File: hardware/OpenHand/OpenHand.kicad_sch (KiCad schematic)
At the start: 0 parts

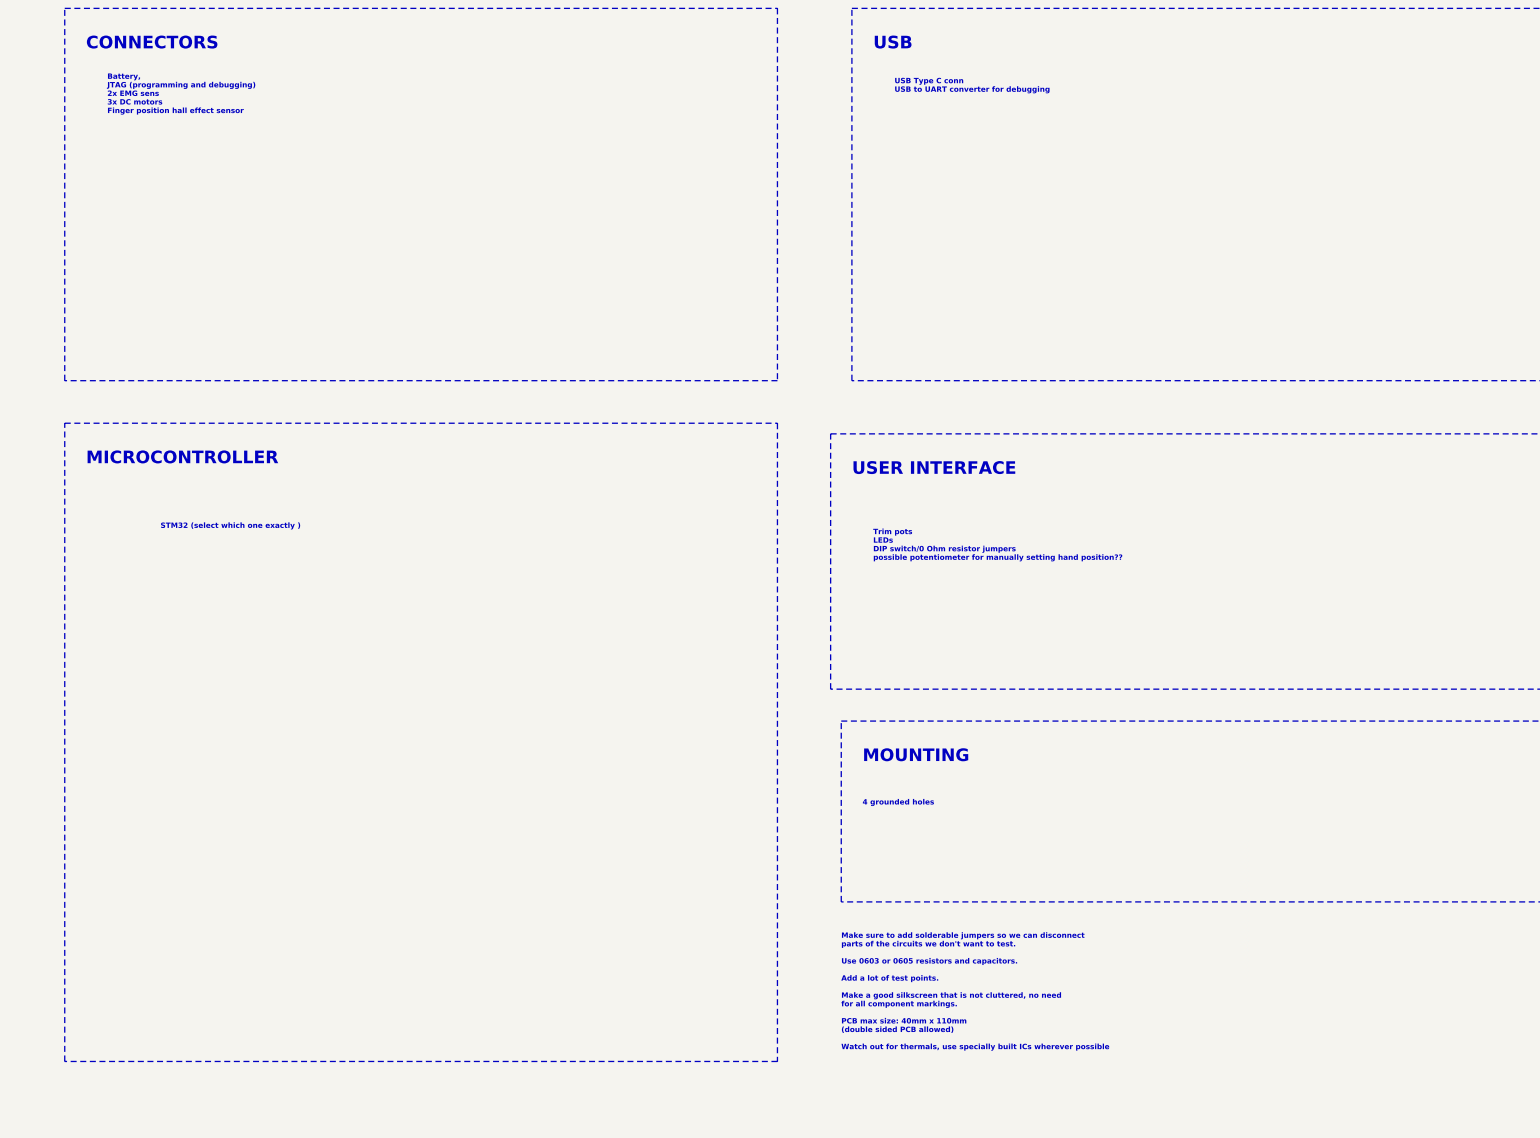
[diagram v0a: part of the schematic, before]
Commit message: Started adding ICs to schematic
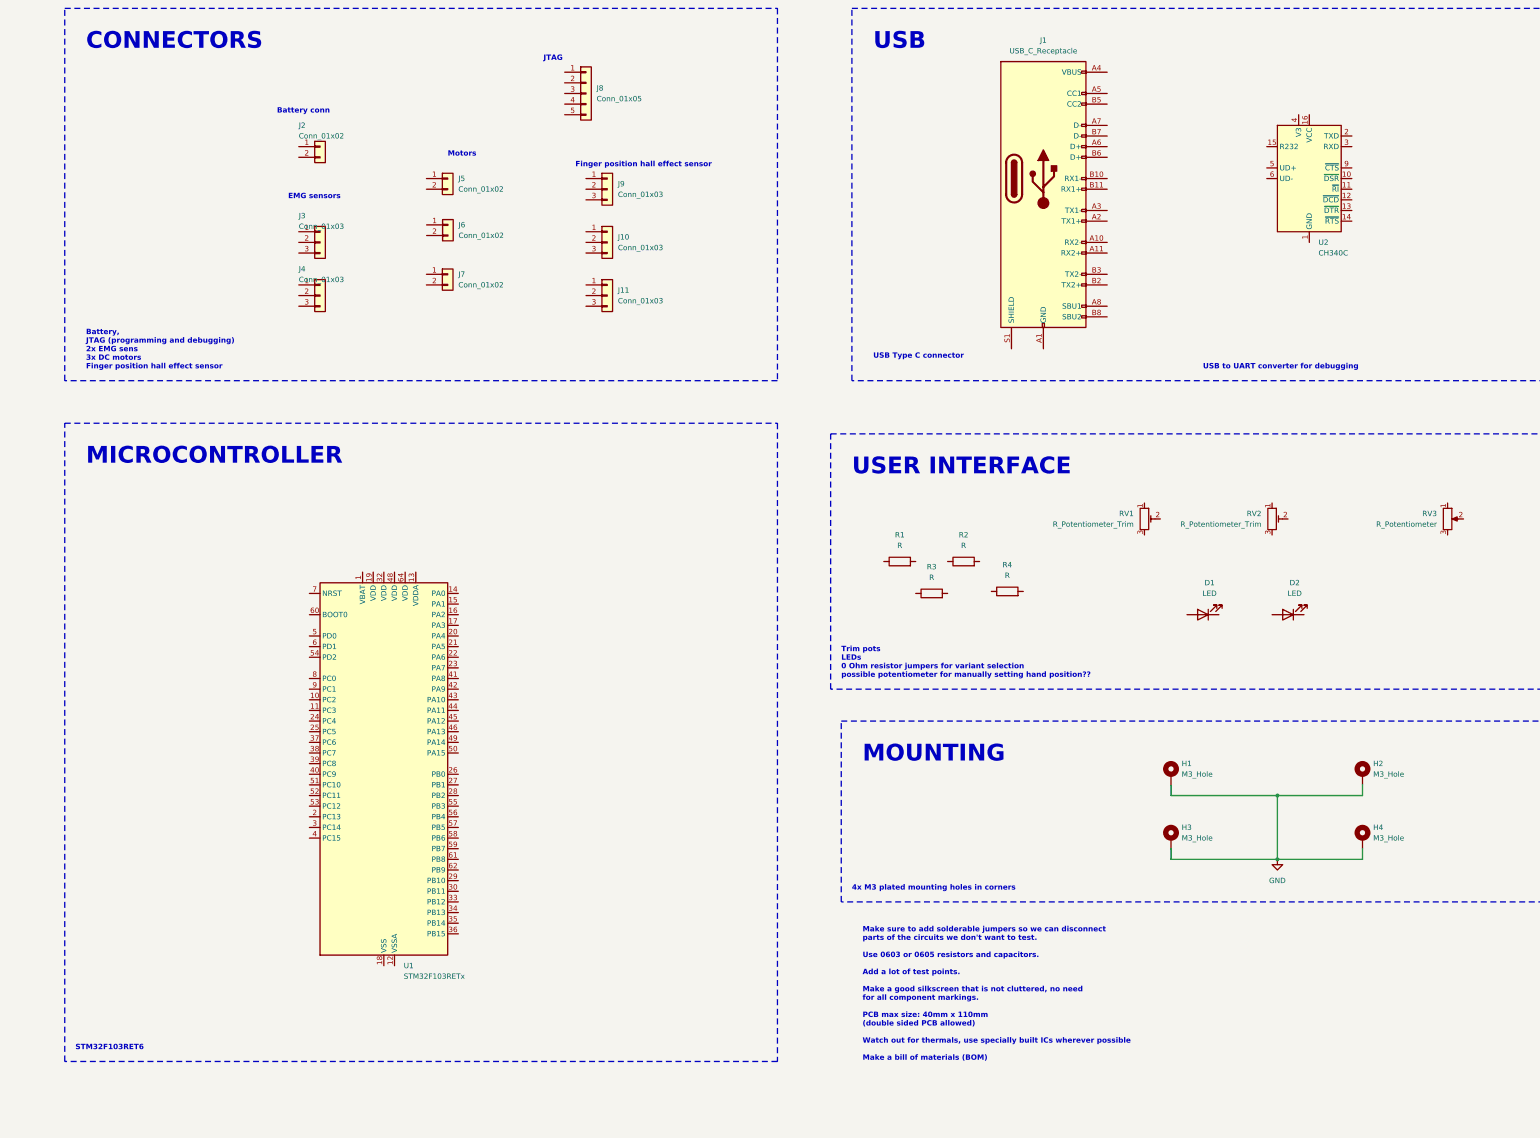
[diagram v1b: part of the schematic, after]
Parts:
- added D1, D2: LED, symbol Device:LED
- added H1, H2, H3, H4: M3_Hole, symbol Mechanical:MountingHole_Pad
- added J1: USB_C_Receptacle, symbol Connector:USB_C_Receptacle
- added J10, J11, J3, J4, J9: Conn_01x03, symbol Connector_Generic:Conn_01x03
- added J2, J5, J6, J7: Conn_01x02, symbol Connector_Generic:Conn_01x02
- added J8: Conn_01x05, symbol Connector_Generic:Conn_01x05
- added R1, R2, R3, R4: R, symbol Device:R
- added RV1, RV2: R_Potentiometer_Trim, symbol Device:R_Potentiometer_Trim
- added RV3: R_Potentiometer, symbol Device:R_Potentiometer
- added U1: STM32F103RETx, Package_QFP:LQFP-64_10x10mm_P0.5mm, symbol MCU_ST_STM32F1:STM32F103RETx
- added U2: CH340C, Package_SO:SOIC-16_3.9x9.9mm_P1.27mm, symbol Interface_USB:CH340C
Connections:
- new net: J1.A1 (GND), J1.A12 (GND), J1.B1 (GND), J1.B12 (GND)
- new net: J1.A4 (VBUS), J1.A9 (VBUS), J1.B4 (VBUS), J1.B9 (VBUS)
- new net: U1.18 (VSS), U1.31 (VSS), U1.47 (VSS), U1.63 (VSS)
- new net GND: H1.1, H2.1, H3.1, H4.1
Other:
- note added: "4x M3 plated mounting holes in corners"
- note added: "Battery conn"
- note added: "EMG sensors"
- note added: "Finger position hall effect sensor"
- note added: "JTAG"
- note added: "Make sure to add solderable jumpers so we can disconnect parts of the circuits we don't want to test. Use 0603 or 0605 resistors and capacitors. Add a lot of test points. Make a good silkscreen that is not cluttered, no need for all component markings. PCB max size: 40mm x 110mm (double sided PCB allowed) Watch out for thermals, use specially built ICs wherever possible Make a bill of materials (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"
- note added: "Motors"
- note added: "STM32F103RET6"
- note added: "Trim pots LEDs 0 Ohm resistor jumpers for variant selection possible potentiometer for manually setting hand position??"
- note added: "USB Type C connector"
- note added: "USB to UART converter for debugging"
- note removed: "4 grounded holes"
- note removed: "Make sure to add solderable jumpers so we can disconnect parts of the circuits we don't want to test. Use 0603 or 0605 resistors and capacitors. Add a lot of test points. Make a good silkscreen that is not cluttered, no need for all component markings. PCB max size: 40mm x 110mm (double sided PCB allowed) Watch out for thermals, use specially built ICs wherever possible"
- note removed: "STM32 (select which one exactly )"
- note removed: "Trim pots LEDs DIP switch/0 Ohm resistor jumpers possible potentiometer for manually setting hand position??"
- note removed: "USB Type C conn USB to UART converter for debugging"

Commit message: Update schematic
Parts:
- removed J8: Conn_01x05, symbol Connector_Generic:Conn_01x05
- added C1: 1u, symbol Device:C
- added C2, C3: 100n, symbol Device:C
- added J9: CONN_JTAG, symbol Connector_Generic:Conn_01x06
- added R5, R6: 1k, symbol Device:R
- added SW1: BTN_RST, symbol Switch:SW_Push
- added SW2: BTN_BOOT, symbol Switch:SW_Push
- added SW3: SW_Push, symbol Switch:SW_Push
- D1: value LED -> RED
- D2: value LED -> GREEN
- J1: renamed from J5; value Conn_01x02 -> CONN_MOTOR_1
- J10: renamed from J4; value Conn_01x03 -> CONN_EMG_2
- J11: value Conn_01x03 -> CONN_POS_3
- J2: renamed from J6; value Conn_01x02 -> CONN_MOTOR_2
- J3: renamed from J2; value Conn_01x02 -> CONN_BATT
- J5: renamed from J9; value Conn_01x03 -> CONN_POS_1
- J6: renamed from J7; value Conn_01x02 -> CONN_MOTOR_3
- J7: renamed from J3; value Conn_01x03 -> CONN_EMG_1
- J8: renamed from J10; value Conn_01x03 -> CONN_POS_2
- RV1: value R_Potentiometer_Trim -> TRIM_POT_1
- RV2: value R_Potentiometer_Trim -> TRIM_POT_2
- RV3: value R_Potentiometer -> POT_1
- renumbered J1 to J4, R3 to R2, R2 to R3, U2 to U1, U1 to U2
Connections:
- net GND is gone; now on net Earth: H1.1, H2.1, H3.1, H4.1
- net Earth: now reaches J8.1 (Pin_1)
- net Earth: now also J10.1 (Pin_1), J11.1 (Pin_1), J3.1 (Pin_1), J4.A1 (GND), J4.A12 (GND), J4.B1 (GND), J4.B12 (GND), J4.S1 (SHIELD), J5.1 (Pin_1), J7.1 (Pin_1), RV1.1, RV2.1, RV3.1, U1.1 (GND), C1.2, C2.2, J9.1 (Pin_1), R5.2, R6.2
- net HALL_SENS_02_S: now reaches J8.2 (Pin_2)
- net HALL_SENS_02_P: now reaches J8.3 (Pin_3)
- net at D1.1 (K): now also R5.1
- net LED_1: now reaches D1.2 (A)
- net +5V: now reaches J4.A4 (VBUS), J4.A9 (VBUS), J4.B4 (VBUS), J4.B9 (VBUS)
- net +5V: now also U1.16 (VCC), C1.1
- net USB_D_P: now reaches J4.A6 (D+)
- net USB_D_P: now also J4.B6 (D+), U1.5 (UD+)
- net USB_D_N: now reaches J4.A7 (D-)
- net USB_D_N: now also J4.B7 (D-), U1.6 (UD-)
- net at U1.13 (~{DTR}): now also C3.1
- net UC_RX: now reaches U1.2 (TXD)
- net UC_TX: now reaches U1.3 (RXD)
- net at U1.4 (V3): now also C2.1
- net MOTOR_1_N: now reaches J1.1 (Pin_1)
- net MOTOR_1_P: now reaches J1.2 (Pin_2)
- net MOTOR_2_N: now reaches J2.1 (Pin_1)
- net MOTOR_2_P: now reaches J2.2 (Pin_2)
- net HALL_SENS_01_S: now reaches J5.2 (Pin_2)
- net HALL_SENS_01_P: now reaches J5.3 (Pin_3)
- net TRIM_POT_2: now reaches RV2.2
- net +3V3: now reaches RV2.3
- net +3V3: now also RV1.3, RV3.3
- net HALL_SENS_03_S: now reaches J11.2 (Pin_2)
- net HALL_SENS_03_P: now reaches J11.3 (Pin_3)
- net at D2.1 (K): now also R6.1
- net LED_2: now reaches D2.2 (A)
- net BAT_P: now reaches J3.2 (Pin_2)
- net EMG_2_N: now reaches J10.2 (Pin_2)
- net EMG_2_P: now reaches J10.3 (Pin_3)
- net TRIM_POT_1: now reaches RV1.2
- net EMG_1_N: now reaches J7.2 (Pin_2)
- net EMG_1_P: now reaches J7.3 (Pin_3)
- net POT_1: now reaches RV3.2
- net MOTOR_3_N: now reaches J6.1 (Pin_1)
- net MOTOR_3_P: now reaches J6.2 (Pin_2)
- new net JTAG_RST: J9.2 (Pin_2)
- new net JTAG_TCK: J9.5 (Pin_5)
- new net JTAG_TDI: J9.3 (Pin_3)
- new net JTAG_TDO: J9.4 (Pin_4)
- new net JTAG_TMS: J9.6 (Pin_6)
- new net UC_RST: C3.2
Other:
- note added: "SMD jumpers for HW variant coding"
- note added: "UC BUTTONS"
- note removed: "Battery, JTAG (programming and debugging) 2x EMG sens 3x DC motors Finger position hall effect sensor"
- note removed: "Trim pots LEDs 0 Ohm resistor jumpers for variant selection possible potentiometer for manually setting hand position??"
- moved on the sheet: D1, D2, H1, H2, H3, H4, J1, J10, J11, J2, J3, J4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

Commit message: working on schematics
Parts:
- removed SW1: BTN_RST, symbol Switch:SW_Push
- removed SW2: BTN_BOOT, symbol Switch:SW_Push
- added JP1, JP2, JP3, JP4, JP5, JP6, JP7, JP8: SolderJumper_2_Open, symbol Jumper:SolderJumper_2_Open
- added R16, R17: 5k1, Resistor_SMD:R_1206_3216Metric, symbol Device:R
- added R6: 10k, Resistor_SMD:R_1206_3216Metric, symbol Device:R
- C1, C2, C3: footprint (none) -> Capacitor_SMD:C_1206_3216Metric
- H1, H2, H3, H4: footprint (none) -> MountingHole:MountingHole_3.2mm_M3_Pad_Via
- R1, R2, R3, R4: value R -> 10k; footprint (none) -> Resistor_SMD:R_1206_3216Metric
- R5: footprint (none) -> Resistor_SMD:R_1206_3216Metric
- R7: renamed from R6; footprint (none) -> Resistor_SMD:R_1206_3216Metric
- renumbered SW3 to SW1
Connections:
- net +3V3: now also R1.1, R2.1, R3.1, R4.1, R6.1
- net Earth: now also SW1.2, JP5.1 (A), JP6.1 (A), JP7.1 (A), JP8.1 (A), R16.2, R17.2
- net at R4.2: now also JP4.2 (B)
- net at J4.A5 (CC1): now also R16.1
- net at J4.B5 (CC2): now also R17.1
- net at R2.2: now also JP2.2 (B)
- net BTN_1: now reaches SW1.1
- net BTN_1: now also R6.2
- net at R1.2: now also JP1.2 (B)
- net at R3.2: now also JP3.2 (B)
- new net HW_REV_1: JP1.1 (A), JP5.2 (B)
- new net HW_REV_2: JP2.1 (A), JP6.2 (B)
- new net HW_REV_3: JP3.1 (A), JP7.2 (B)
- new net HW_REV_4: JP4.1 (A), JP8.2 (B)
- no-connect marks 0 -> 11
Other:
- note added: "- Make sure to add solderable jumpers so we can disconnect parts of the circuits we don't want to test (SolderJumper_2_Bridged) - Use 0805 resistors and capacitors wherever possible (standard values: 1k, 10k...) - Add a lot of test points, and make them somewhat small - Make a good silkscreen that is not cluttered, no need for all component markings. - Watch out for thermals, especially with moto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"
- note added: "Debug LEDs"
- note added: "For resetting/programming the board"
- note added: "PCB manufacturing capabilities: - min trace width 0.2mm and spacing 0.2mm - min via hole size/diameter: 0.3mm / 0.5mm"
- note added: "Potentiometers"
- note added: "Push button"
- note added: "Solder jumpers for HW variant coding"
- note added: "YT: Aesthetic PCB Design Tips - Phil's Lab #84"
- note added: "YT: STM32 PCB Design - Complete Walkthrough - Phil's Lab #41"
- note removed: "Make sure to add solderable jumpers so we can disconnect parts of the circuits we don't want to test. Use 0603 or 0605 resistors and capacitors. Add a lot of test points. Make a good silkscreen that is not cluttered, no need for all component markings. PCB max size: 40mm x 110mm (double sided PCB allowed) Watch out for thermals, use specially built ICs wherever possible Make a bill of materials (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"
- note removed: "SMD jumpers for HW variant coding"
- company: Fungdale -> (none)
- moved on the sheet: D1, D2, R5, R7, RV1, RV2, RV3, SW1

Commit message: Minor updates to schm
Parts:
- added C4: 100n, Capacitor_SMD:C_1206_3216Metric, symbol Device:C
- added J11: CONN_FDBK_2, symbol Connector_Generic:Conn_01x02
- added J7: CONN_FDBK_1, symbol Connector_Generic:Conn_01x02
- added Q1, Q2: 2N7002, Package_TO_SOT_SMD:SOT-23, symbol Transistor_FET:2N7002
- added R3, R4: 1k, symbol Device:R
- added SW2: BTN_RST, symbol Switch:SW_Push
- added SW3: BTN_BOOT, symbol Switch:SW_Push
- D1, D2: footprint (none) -> LED_SMD:LED_0805_2012Metric
- J4: value USB_C_Receptacle -> USB_C_CONN; footprint (none) -> Connector_USB:USB_C_Receptacle_G-Switch_GT-USB-7010ASV
- JP1, JP2, JP3, JP4, JP5, JP6, JP7, JP8: footprint (none) -> Jumper:SolderJumper-2_P1.3mm_Open_RoundedPad1.0x1.5mm
- renumbered J9 to J10, J10 to J12, J11 to J13, J7 to J8, J8 to J9, R16 to R1, R6 to R10, R7 to R11, R17 to R2, R1 to R5, R2 to R6, R3 to R7, R4 to R8, R5 to R9
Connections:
- net Earth: now also C3.2, C4.2, SW2.2, SW3.2
- net UC_RST: now also C3.1, U2.7 (NRST), Q1.3 (D), SW2.1; no longer C3.2
- net at U1.13 (~{DTR}): now also Q2.2 (S), R3.1; no longer C3.1
- net at U1.14 (~{RTS}): now also Q1.2 (S), R4.1
- net UC_BOOT: now reaches U2.60 (BOOT0)
- net UC_BOOT: now also C4.1, Q2.3 (D), SW3.1
- net BAT_P renamed +BATT
- new net: Q1.1 (G), R3.2
- new net: Q2.1 (G), R4.2
- new net FDBK_MOTOR_1_N: J7.1 (Pin_1)
- new net FDBK_MOTOR_1_P: J7.2 (Pin_2)
- new net FDBK_MOTOR_2_N: J11.1 (Pin_1)
- new net FDBK_MOTOR_2_P: J11.2 (Pin_2)
- no-connect marks 11 -> 15
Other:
- note added: "Battery"
- note added: "Haptic feedback motors"
- note removed: "Battery conn"
- moved on the sheet: C1, C2, H1, H2, H3, H4, J1, J10, J12, J13, J2, J3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
